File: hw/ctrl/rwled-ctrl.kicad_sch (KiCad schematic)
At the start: 47 parts, among them J21 batt, J31 USB_B_Micro, J61 led-a, J62 led-b, J63 led-c, J64 led-d, Q31 UMH3N, Q51 ML2502, Q52 ML2502, Q61 ML5203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

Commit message: hw ctrl - плата - расставлены элементы
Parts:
- added C61: 10μF, Capacitor_SMD:C_0805_2012Metric, symbol Device:C
- added D22: 1N5819, Diode_SMD:D_SOD-323, symbol Device:D
- added D24, D25: SS56, Diode_SMD:D_SMA, symbol Device:D
- added J21: batt-chg, Connector_AMASS:AMASS_XT30U-M_1x02_P5.0mm_Vertical, symbol Connector_Generic:Conn_01x02
- added J66: batt-cd, Connector_AMASS:AMASS_XT30U-F_1x02_P5.0mm_Vertical, symbol Connector_Generic:Conn_01x02
- added Q61: IRF4905STRLPBF, Package_TO_SOT_SMD:TO-263-2, symbol Device:Q_PMOS_GDS
- added R61: 10k, Resistor_SMD:R_0805_2012Metric, symbol Device:R
- D51, D52: footprint LED_THT:LED_D10.0mm -> LED_THT:LED_D3.0mm
- J61, J62, J63, J64: footprint (none) -> Connector_JST:JST_XH_S3B-XH-A_1x03_P2.50mm_Horizontal
- J65: renamed from J21; value batt -> batt-ab; footprint (none) -> Connector_AMASS:AMASS_XT30U-F_1x02_P5.0mm_Vertical
- Q62: renamed from Q61; value ML5203 -> IRF4905STRLPBF; footprint Package_TO_SOT_SMD:SOT-23 -> Package_TO_SOT_SMD:TO-263-2; symbol Device:Q_PMOS_GSD -> Device:Q_PMOS_GDS
- renumbered C61 to C62, D22 to D23, R61 to R62, R62 to R63, R63 to R64
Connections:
- net +5V: now also D22.1 (K)
- net GND: now also C62.1, J65.1 (Pin_1), C61.2, J21.1 (Pin_1), J66.1 (Pin_1); no longer C62.2, J65.2 (Pin_2)
- net s-boot: now also Q31.3 (C2); no longer Q31.1 (E1)
- net s-en: now also Q31.6 (C1); no longer Q31.4 (E2)
- net at Q62.1 (G), Q?.3 (C), R62.1: now also Q61.1 (G), R61.1
- removed net VCC: D21.2 (A), J65.1 (Pin_1), Q62.2 (S), R62.2
- removed net v-led: C62.1, J61.1 (Pin_1), J62.1 (Pin_1), J63.1 (Pin_1), J64.1 (Pin_1), Q62.3 (D)
- new net: Q31.1 (E1), Q31.5 (B2), U31.24 (~{RTS})
- new net: Q31.2 (B1), Q31.4 (E2), U31.28 (~{DTR})
- new net: D24.2 (A), D25.2 (A), J21.2 (Pin_2)
- new net +BATT-AB: D21.2 (A), D24.1 (K), J65.2 (Pin_2), Q61.3 (S), R61.2
- new net +BATT-CD: D22.2 (A), D25.1 (K), J66.2 (Pin_2), Q62.3 (S), R62.2
- new net v-led-ab: C61.1, J61.1 (Pin_1), J62.1 (Pin_1), Q61.2 (D)
- new net v-led-cd: C62.2, J63.1 (Pin_1), J64.1 (Pin_1), Q62.2 (D)
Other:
- moved on the sheet: C62, D23, J61, J62, J63, J64, J65, Q31A, Q31B, Q62, Q?, R62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

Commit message: hw ctrl - плата доразведена
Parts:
- removed Q51, Q52: ML2502, Package_TO_SOT_SMD:SOT-23, symbol Device:Q_NMOS_GSD
- removed Q?: c1815, Package_TO_SOT_SMD:SOT-23, symbol Device:Q_NPN_BEC
- removed R52, R55, R63: 510, Resistor_SMD:R_0805_2012Metric, symbol Device:R
- removed R53, R56: 100k, Resistor_SMD:R_0805_2012Metric, symbol Device:R
- removed U31: CP2102, Package_DFN_QFN:QFN-28-1EP_5x5mm_P0.5mm_EP3.35x3.35mm, symbol Interface_USB:CP2102N-Axx-xQFN28
- added Q63, Q64: UMH3N, Package_TO_SOT_SMD:SOT-363_SC-70-6, symbol Transistor_BJT:UMH3N
- added U31: CP2104, Package_DFN_QFN:QFN-24-1EP_4x4mm_P0.5mm_EP2.6x2.6mm, symbol Interface_USB:CP2104
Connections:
- net +3.3V: now also R13.1; no longer R13.2
- net GND: now also C12.2, R34.1, Q63.4 (E2), Q63.6 (C1), Q64.4 (E2), Q64.6 (C1), U31.2 (GND), U31.25 (GND); no longer C12.1, R34.2
- net VBUS: now also R31.2, U31.7 (REGIN), U31.8 (VBUS); no longer R31.1
- net btn: now also R13.2; no longer R13.1
- net ldata-a: now also U11.11 (IO26); no longer U11.10 (IO25)
- net ldata-b: now also U11.12 (IO27); no longer U11.11 (IO26)
- net ldata-c: now also U11.10 (IO25); no longer U11.12 (IO27)
- net led-g: now also Q64.2 (B1)
- net led-r: now also Q64.5 (B2)
- net leden: now also R64.1, Q63.2 (B1), Q63.5 (B2)
- net s-en: now also C12.1; no longer C12.2
- net s-rx: now also R32.1; no longer R32.2
- net s-tx: now also R33.1; no longer R33.2
- net at Q62.1 (G), R62.1: now also Q63.3 (C2); no longer Q61.1 (G), R61.1
- net at R51.1: now also Q64.3 (C2)
- net at R54.1: now also Q64.1 (E1)
- net at Q31.1 (E1), Q31.5 (B2): now also U31.19 (~{RTS})
- net at Q31.2 (B1), Q31.4 (E2): now also U31.23 (~{DTR})
- net at J31.3 (D+): now also U31.3 (D+)
- net at J31.2 (D-): now also U31.4 (D-)
- new net: Q61.1 (G), Q63.1 (E1), R61.1
- new net: R32.2, U31.21 (TXD)
- new net: R33.2, U31.20 (RXD)
- new net: R34.2, U31.17 (SUSPEND)
- new net: U31.5 (VIO), U31.6 (VDD)
- new net: R31.1, U31.9 (~{RST})
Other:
- moved on the sheet: C12, D51, D52, R13, R31, R32, R33, R34, R51, R54, R64

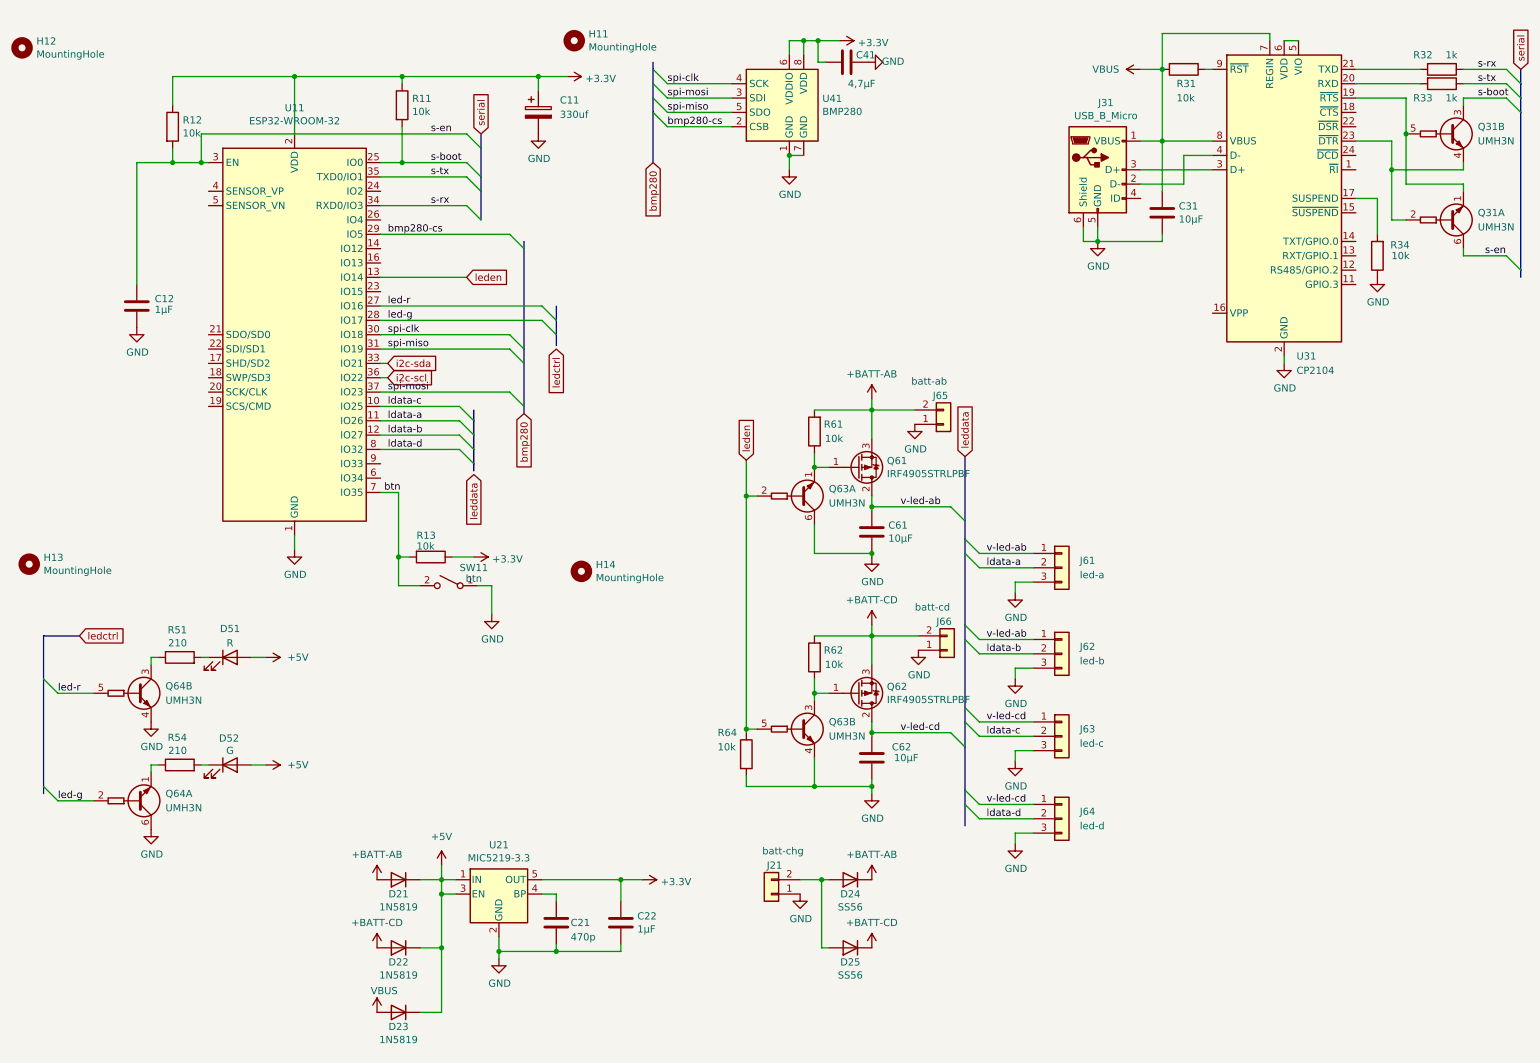
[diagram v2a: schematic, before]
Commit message: hw - доработки платы под oled-дисплей
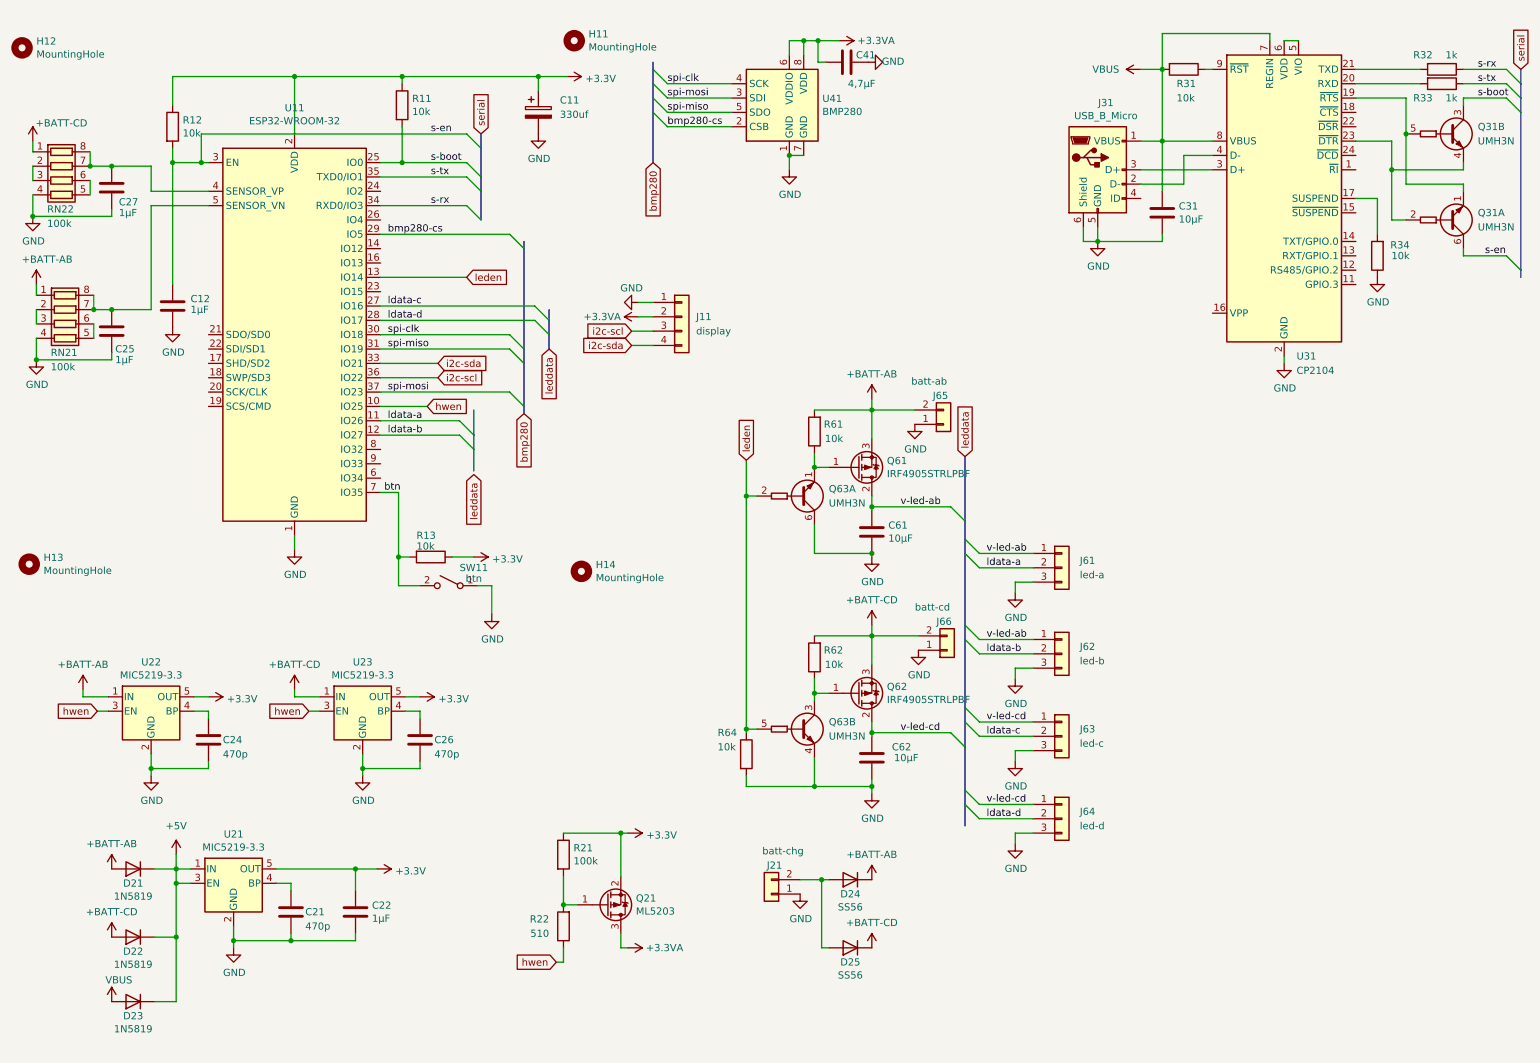
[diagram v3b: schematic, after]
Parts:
- removed D51: R, LED_THT:LED_D3.0mm, symbol Device:LED
- removed D52: G, LED_THT:LED_D3.0mm, symbol Device:LED
- removed Q64: UMH3N, Package_TO_SOT_SMD:SOT-363_SC-70-6, symbol Transistor_BJT:UMH3N
- removed R51, R54: 210, Resistor_SMD:R_1206_3216Metric, symbol Device:R
- added C24, C26: 470p, Capacitor_SMD:C_0805_2012Metric, symbol Device:C
- added C25, C27: 1μF, Capacitor_SMD:C_0805_2012Metric, symbol Device:C
- added J11: display, Connector_PinHeader_2.54mm:PinHeader_1x04_P2.54mm_Vertical, symbol Connector_Generic:Conn_01x04
- added Q21: ML5203, Package_TO_SOT_SMD:SOT-23, symbol Device:Q_PMOS_GSD
- added R21: 100k, Resistor_SMD:R_0805_2012Metric, symbol Device:R
- added R22: 510, Resistor_SMD:R_0805_2012Metric, symbol Device:R
- added RN21, RN22: 100k, Resistor_SMD:R_Array_Convex_4x0603, symbol Device:R_Pack04
- added U22, U23: MIC5219-3.3, Package_TO_SOT_SMD:SOT-23-5, symbol Regulator_Linear:MIC5219-3.3YM5
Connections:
- net led-g is gone; now on net ldata-d: U11.28 (IO17)
- net led-r is gone; now on net ldata-c: U11.27 (IO16)
- net +3.3V: now also Q21.2 (S), R21.1, U22.5 (OUT), U23.5 (OUT); no longer C41.1, U41.6 (VDDIO), U41.8 (VDD)
- net +BATT-AB: now also RN21.1 (R1.1), U22.1 (IN)
- net +BATT-CD: now also RN22.1 (R1.1), U23.1 (IN)
- net GND: now also C24.2, C25.2, C26.2, C27.2, J11.1 (Pin_1), RN21.4 (R4.1), RN22.4 (R4.1), U22.2 (GND), U23.2 (GND)
- net i2c-scl: now also J11.3 (Pin_3)
- net i2c-sda: now also J11.4 (Pin_4)
- net ldata-c: no longer U11.10 (IO25)
- net ldata-d: no longer U11.8 (IO32)
- net at U11.4 (SENSOR_VP): now also C27.1, RN22.7 (R2.2), RN22.8 (R1.2)
- net at U11.5 (SENSOR_VN): now also C25.1, RN21.7 (R2.2), RN21.8 (R1.2)
- new net: C26.1, U23.4 (BP)
- new net: Q21.1 (G), R21.2, R22.2
- new net: C24.1, U22.4 (BP)
- new net: RN21.2 (R2.1), RN21.3 (R3.1)
- new net: RN21.5 (R4.2), RN21.6 (R3.2)
- new net: RN22.2 (R2.1), RN22.3 (R3.1)
- new net: RN22.5 (R4.2), RN22.6 (R3.2)
- new net +3.3VA: C41.1, J11.2 (Pin_2), Q21.3 (D), U41.6 (VDDIO), U41.8 (VDD)
- new net hwen: R22.1, U11.10 (IO25), U22.3 (EN), U23.3 (EN)
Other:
- moved on the sheet: C12, C21, C22, D21, D22, D23, U21

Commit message: hw - архив доработанных и отправленных в заказ плат
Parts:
- removed C24, C26: 470p, Capacitor_SMD:C_0805_2012Metric, symbol Device:C
- removed U22, U23: MIC5219-3.3, Package_TO_SOT_SMD:SOT-23-5, symbol Regulator_Linear:MIC5219-3.3YM5
- added R23: 10k, Resistor_SMD:R_0805_2012Metric, symbol Device:R
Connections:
- net +5V: now also R23.1; no longer U21.3 (EN)
- net GND: now also Q63.1 (E1); no longer Q63.6 (C1)
- net at Q61.1 (G), R61.1: now also Q63.6 (C1); no longer Q63.1 (E1)
- new net: R23.2, U21.3 (EN)
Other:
- moved on the sheet: D21, D22, D23
